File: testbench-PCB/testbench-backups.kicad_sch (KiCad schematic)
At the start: 6 parts, among them U1 ATmega2561-16A, U2 Rotary_encoder_switch_module, U3 Thermistor_module

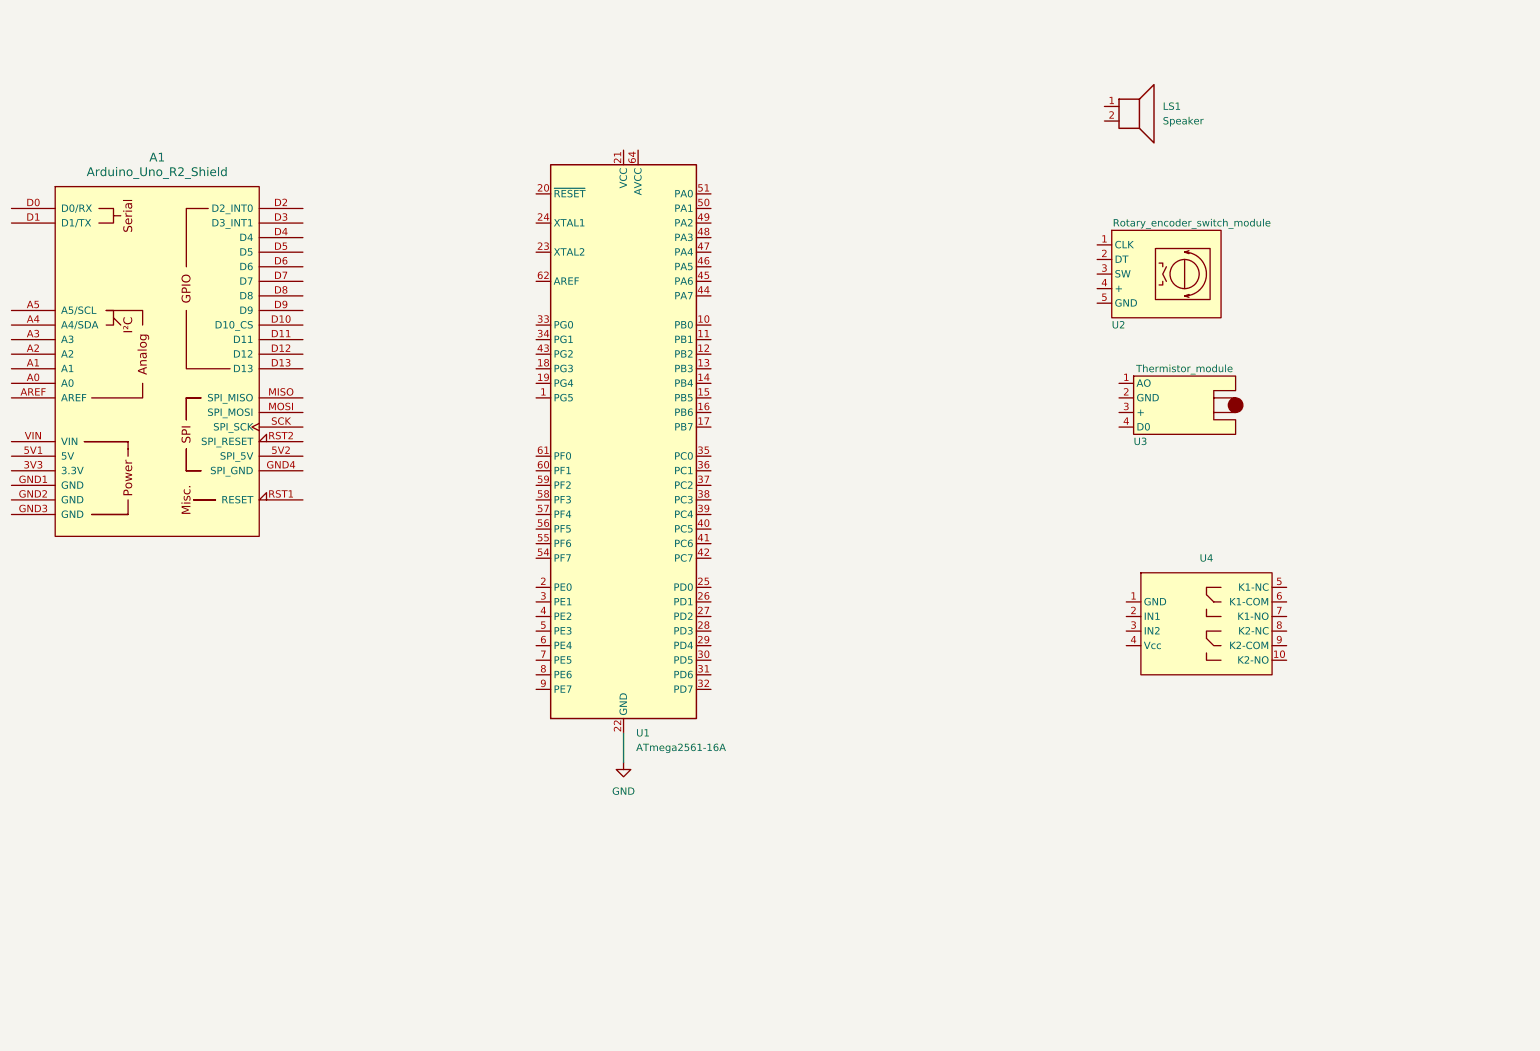
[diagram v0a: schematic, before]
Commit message: Added the rest of kit modules.
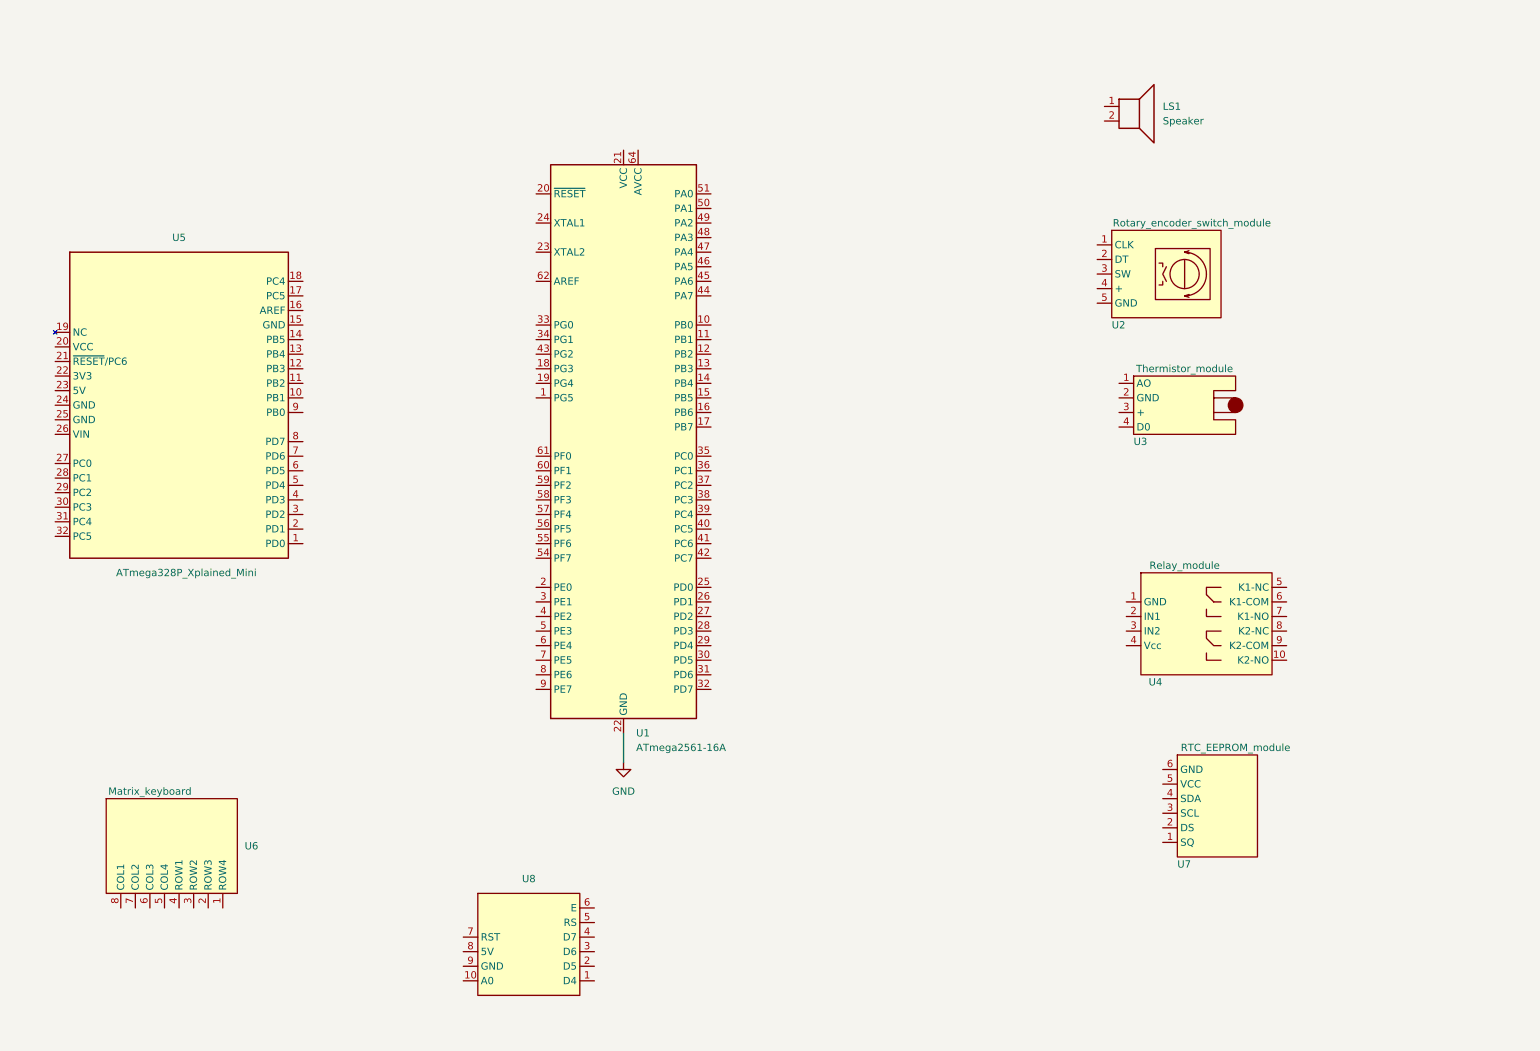
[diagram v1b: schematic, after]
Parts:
- removed A1: Arduino_Uno_R2_Shield, PCM_arduino-library:Arduino_Uno_R2_Shield, symbol PCM_arduino-library:Arduino_Uno_R2_Shield
- added U5: ATmega328P_Xplained_Mini, kit_modules:ATmega328P_Xplained_Mini, symbol kit_modules:ATmega328P_Xplained_mini
- added U6: Matrix_keyboard, symbol kit_modules:matrix_keyboard
- added U7: RTC_EEPROM_module, symbol kit_modules:RTC_module
- added U8: ~, symbol kit_modules:LCD_module
- U4: value ~ -> Relay_module
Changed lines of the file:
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@@
     )
   )
-  (symbol (lib_id "kit_modules:thermistor_module") (at 217.17 80.01 0) (unit 1)
-    (in_bom yes) (on_board yes) (dnp no)
-    (property "Reference" "U3" (at 219.71 86.36 0)
-      (effects (font (size 1.27 1.27)) (justify left))
-    )
-    (property "Value" "Thermistor_module" (at 228.6 73.66 0)
-      (effects (font (size 1.27 1.27)))
-    )
-    (property "Footprint" "" (at 217.17 80.01 0)
-      (effects (font (size 1.27 1.27)) hide)
-    )
-    (property "Datasheet" "" (at 217.17 80.01 0)
-      (effects (font (size 1.27 1.27)) hide)
-    )
-    (pin "1")
-    (pin "2")
-    (pin "3")
-    (pin "4")
-    (instances
-      (project "testbench-backups"
-        (path "/3ac6901d-218d-4b34-8c4a-bf7c417c33bc"
-          (reference "U3") (unit 1)
-        )
-      )
-    )
-  )
-  (symbol (lib_id "MCU_Microchip_ATmega:ATmega2561-16A") (at 130.81 86.36 0) (unit 1)
-    (in_bom yes) (on_board yes) (dnp no) (fields_autoplaced)
-    (property "Reference" "U1" (at 133.0041 137.16 0)
-      (effects (font (size 1.27 1.27)) (justify left))
-    )
-    (property "Value" "ATmega2561-16A" (at 133.0041 139.7 0)
-      (effects (font (size 1.27 1.27)) (justify left))
-    )
-    (property "Footprint" "Package_QFP:TQFP-64_14x14mm_P0.8mm" (at 130.81 86.36 0)
-      (effects (font (size 1.27 1.27) italic) hide)
-    )
-    (property "Datasheet" "http://ww1.microchip.com/downloads/en/DeviceDoc/Atmel-2549-8-bit-AVR-Microcontroller-ATmega640-1280-1281-2560-2561_datasheet.pdf" (at 130.81 86.36 0)
+  (symbol (lib_id "kit_modules:ATmega328P_Xplained_mini") (at 44.45 44.45 0) (unit 1)
+    (in_bom yes) (on_board yes) (dnp no)
+    (property "Reference" "U5" (at 53.34 50.8 0)
+      (effects (font (size 1.27 1.27)))
+    )
+    (property "Value" "ATmega328P_Xplained_Mini" (at 54.61 109.22 0)
+      (effects (font (size 1.27 1.27)))
+    )
+    (property "Footprint" "kit_modules:ATmega328P_Xplained_Mini" (at 38.1 53.34 0)
+      (effects (font (size 1.27 1.27)) hide)
+    )
+    (property "Datasheet" "" (at 38.1 53.34 0)
       (effects (font (size 1.27 1.27)) hide)
     )
@@
     (pin "31")
     (pin "32")
+    (pin "4")
+    (pin "5")
+    (pin "6")
+    (pin "7")
+    (pin "8")
+    (pin "9")
+    (instances
+      (project "testbench-backups"
+        (path "/3ac6901d-218d-4b34-8c4a-bf7c417c33bc"
+          (reference "U5") (unit 1)
+        )
+      )
+    )
+  )
+  (symbol (lib_id "kit_modules:thermistor_module") (at 217.17 80.01 0) (unit 1)
+    (in_bom yes) (on_board yes) (dnp no)
+    (property "Reference" "U3" (at 219.71 86.36 0)
+      (effects (font (size 1.27 1.27)) (justify left))
+    )
+    (property "Value" "Thermistor_module" (at 228.6 73.66 0)
+      (effects (font (size 1.27 1.27)))
+    )
+    (property "Footprint" "" (at 217.17 80.01 0)
+      (effects (font (size 1.27 1.27)) hide)
+    )
+    (property "Datasheet" "" (at 217.17 80.01 0)
+      (effects (font (size 1.27 1.27)) hide)
+    )
+    (pin "1")
+    (pin "2")
+    (pin "3")
+    (pin "4")
+    (instances
+      (project "testbench-backups"
+        (path "/3ac6901d-218d-4b34-8c4a-bf7c417c33bc"
+          (reference "U3") (unit 1)
+        )
+      )
+    )
+  )
+  (symbol (lib_id "kit_modules:RTC_module") (at 224.79 156.21 0) (unit 1)
+    (in_bom yes) (on_board yes) (dnp no)
+    (property "Reference" "U7" (at 227.33 160.02 0)
+      (effects (font (size 1.27 1.27)) (justify left))
+    )
+    (property "Value" "RTC_EEPROM_module" (at 237.49 139.7 0)
+      (effects (font (size 1.27 1.27)))
+    )
+    (property "Footprint" "" (at 228.6 160.02 0)
+      (effects (font (size 1.27 1.27)) hide)
+    )
+    (property "Datasheet" "" (at 228.6 160.02 0)
+      (effects (font (size 1.27 1.27)) hide)
+    )
+    (pin "1")
+    (pin "2")
+    (pin "3")
+    (pin "4")
+    (pin "5")
+    (pin "6")
+    (instances
+      (project "testbench-backups"
+        (path "/3ac6901d-218d-4b34-8c4a-bf7c417c33bc"
+          (reference "U7") (unit 1)
+        )
+      )
+    )
+  )
+  (symbol (lib_id "MCU_Microchip_ATmega:ATmega2561-16A") (at 130.81 86.36 0) (unit 1)
+    (in_bom yes) (on_board yes) (dnp no) (fields_autoplaced)
+    (property "Reference" "U1" (at 133.0041 137.16 0)
+      (effects (font (size 1.27 1.27)) (justify left))
+    )
+    (property "Value" "ATmega2561-16A" (at 133.0041 139.7 0)
+      (effects (font (size 1.27 1.27)) (justify left))
+    )
+    (property "Footprint" "Package_QFP:TQFP-64_14x14mm_P0.8mm" (at 130.81 86.36 0)
+      (effects (font (size 1.27 1.27) italic) hide)
+    )
+    (property "Datasheet" "http://ww1.microchip.com/downloads/en/DeviceDoc/Atmel-2549-8-bit-AVR-Microcontroller-ATmega640-1280-1281-2560-2561_datasheet.pdf" (at 130.81 86.36 0)
+      (effects (font (size 1.27 1.27)) hide)
+    )
+    (pin "1")
+    (pin "10")
+    (pin "11")
+    (pin "12")
+    (pin "13")
+    (pin "14")
+    (pin "15")
+    (pin "16")
+    (pin "17")
+    (pin "18")
+    (pin "19")
+    (pin "2")
+    (pin "20")
+    (pin "21")
+    (pin "22")
+    (pin "23")
+    (pin "24")
+    (pin "25")
+    (pin "26")
+    (pin "27")
+    (pin "28")
+    (pin "29")
+    (pin "3")
+    (pin "30")
+    (pin "31")
+    (pin "32")
     (pin "33")
     (pin "34")
@@
     )
   )
+  (symbol (lib_id "kit_modules:LCD_module") (at 102.87 182.88 0) (unit 1)
+    (in_bom yes) (on_board yes) (dnp no) (fields_autoplaced)
+    (property "Reference" "U8" (at 114.3 162.56 0)
+      (effects (font (size 1.27 1.27)))
+    )
+    (property "Value" "~" (at 106.68 184.15 0)
+      (effects (font (size 1.27 1.27)))
+    )
+    (property "Footprint" "" (at 106.68 184.15 0)
+      (effects (font (size 1.27 1.27)) hide)
+    )
+    (property "Datasheet" "" (at 106.68 184.15 0)
+      (effects (font (size 1.27 1.27)) hide)
+    )
+    (pin "1")
+    (pin "10")
+    (pin "2")
+    (pin "3")
+    (pin "4")
+    (pin "5")
+    (pin "6")
+    (pin "7")
+    (pin "8")
+    (pin "9")
+    (instances
+      (project "testbench-backups"
+        (path "/3ac6901d-218d-4b34-8c4a-bf7c417c33bc"
+          (reference "U8") (unit 1)
+        )
+      )
+    )
+  )
   (symbol (lib_id "kit_modules:relay_module") (at 218.44 118.11 0) (unit 1)
-    (in_bom yes) (on_board yes) (dnp no) (fields_autoplaced)
-    (property "Reference" "U4" (at 232.41 106.68 0)
-      (effects (font (size 1.27 1.27)))
-    )
-    (property "Value" "~" (at 218.44 121.92 0)
+    (in_bom yes) (on_board yes) (dnp no)
+    (property "Reference" "U4" (at 223.52 128.27 0)
+      (effects (font (size 1.27 1.27)))
+    )
+    (property "Value" "Relay_module" (at 228.6 107.95 0)
       (effects (font (size 1.27 1.27)))
     )
@@
     )
   )
-  (symbol (lib_id "PCM_arduino-library:Arduino_Uno_R2_Shield") (at 49.53 72.39 0) (unit 1)
-    (in_bom yes) (on_board yes) (dnp no) (fields_autoplaced)
-    (property "Reference" "A1" (at 49.53 36.83 0)
-      (effects (font (size 1.524 1.524)))
-    )
-    (property "Value" "Arduino_Uno_R2_Shield" (at 49.53 39.37 0)
-      (effects (font (size 1.524 1.524)))
-    )
-    (property "Footprint" "PCM_arduino-library:Arduino_Uno_R2_Shield" (at 49.53 110.49 0)
-      (effects (font (size 1.524 1.524)) hide)
-    )
-    (property "Datasheet" "https://startingelectronics.org/articles/arduino/uno-r3-r2-differences/" (at 49.53 106.68 0)
-      (effects (font (size 1.524 1.524)) hide)
-    )
-    (pin "3V3")
-    (pin "5V1")
-    (pin "5V2")
-    (pin "A0")
-    (pin "A1")
-    (pin "A2")
-    (pin "A3")
-    (pin "A4")
-    (pin "A5")
-    (pin "AREF")
-    (pin "D0")
-    (pin "D1")
-    (pin "D10")
-    (pin "D11")
-    (pin "D12")
-    (pin "D13")
-    (pin "D2")
-    (pin "D3")
-    (pin "D4")
-    (pin "D5")
-    (pin "D6")
-    (pin "D7")
-    (pin "D8")
-    (pin "D9")
-    (pin "GND1")
-    (pin "GND2")
-    (pin "GND3")
-    (pin "GND4")
-    (pin "MISO")
-    (pin "MOSI")
-    (pin "RST1")
-    (pin "RST2")
-    (pin "SCK")
-    (pin "VIN")
-    (instances
-      (project "testbench-backups"
-        (path "/3ac6901d-218d-4b34-8c4a-bf7c417c33bc"
-          (reference "A1") (unit 1)
-        )
-      )
+  (symbol (lib_id "kit_modules:matrix_keyboard") (at 40.64 165.1 0) (unit 1)
+    (in_bom yes) (on_board yes) (dnp no)
+    (property "Reference" "U6" (at 64.77 156.845 0)
+      (effects (font (size 1.27 1.27)) (justify left))
+    )
+    (property "Value" "Matrix_keyboard" (at 48.26 147.32 0)
+      (effects (font (size 1.27 1.27)))
+    )
+    (property "Footprint" "" (at 40.64 165.1 0)
+      (effects (font (size 1.27 1.27)) hide)
+    )
+    (property "Datasheet" "" (at 40.64 165.1 0)
+      (effects (font (size 1.27 1.27)) hide)
+    )
+    (pin "1")
+    (pin "2")
+    (pin "3")
+    (pin "4")
+    (pin "5")
+    (pin "6")
+    (pin "7")
+    (pin "8")
+    (instances
+      (project "testbench-backups"
+        (path "/3ac6901d-218d-4b34-8c4a-bf7c417c33bc"
+          (reference "U6") (unit 1)
+        )
+      )

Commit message: Added minimal MCU circuit, power supply from USB.
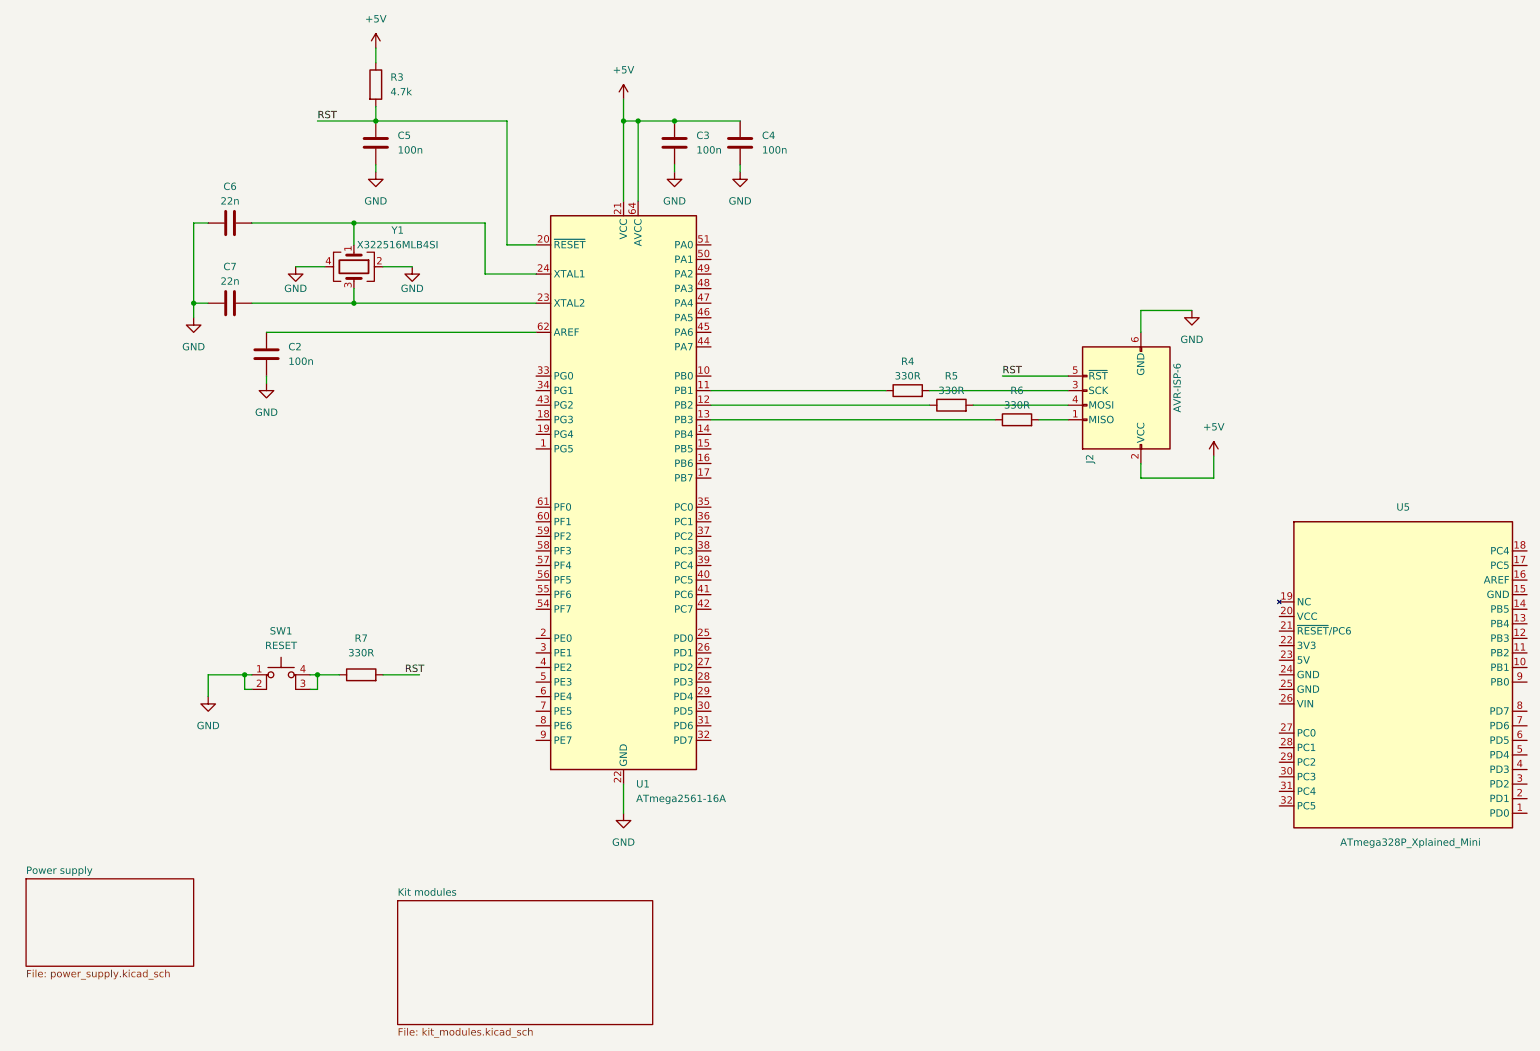
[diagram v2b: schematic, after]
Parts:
- removed LS1: Speaker, symbol Device:Speaker
- removed U2: Rotary_encoder_switch_module, symbol kit_modules:encoder_module
- removed U3: Thermistor_module, symbol kit_modules:thermistor_module
- removed U4: Relay_module, symbol kit_modules:relay_module
- removed U6: Matrix_keyboard, symbol kit_modules:matrix_keyboard
- removed U7: RTC_EEPROM_module, symbol kit_modules:RTC_module
- removed U8: ~, symbol kit_modules:LCD_module
- added C2, C3, C4, C5: 100n, symbol Device:C
- added C6, C7: 22n, symbol Device:C
- added J2: AVR-ISP-6, symbol Connector:AVR-ISP-6
- added R3: 4.7k, symbol Device:R
- added R4, R5, R6, R7: 330R, symbol Device:R
- added SW1: RESET, symbol Switch:SW_MEC_5E
- added Y1: X322516MLB4SI, symbol Device:Crystal_GND24
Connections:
- net GND: now also C2.2, C3.2, C4.2, C5.2, C6.1, C7.1, J2.6 (GND), SW1.1, SW1.2, Y1.2, Y1.4
- net at U1.11 (PB1): now also R4.1
- net at U1.12 (PB2): now also R5.1
- net at U1.13 (PB3): now also R6.1
- net RST: now reaches U1.20 (~{RESET})
- net RST: now also C5.1, J2.5 (~{RST}), R3.2, R7.2
- net +5V: now reaches U1.21 (VCC), U1.52 (VCC)
- net +5V: now also U1.64 (AVCC), C3.1, C4.1, J2.2 (VCC), R3.1
- net at U1.23 (XTAL2): now also C7.2, Y1.3
- net at U1.24 (XTAL1): now also C6.2, Y1.1
- net at U1.62 (AREF): now also C2.1
- new net: J2.3 (SCK), R4.2
- new net: R7.1, SW1.3 (K), SW1.4 (A)
- new net: J2.1 (MISO), R6.2
- new net: J2.4 (MOSI), R5.2
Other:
- added sheet Kit modules (kit_modules.kicad_sch)
- added sheet Power supply (power_supply.kicad_sch)
- moved on the sheet: U1, U5
